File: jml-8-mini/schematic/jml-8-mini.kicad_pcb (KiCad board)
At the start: 4 copper layers, 136.4 x 81.5 mm, 50 parts, among them J1 BarrelJack, J2 SIO CHB, J3 UART, J4 CTC Extra Lines, J5 Address Decoding, J6 Z80 Lines, SW1 Reset, SW2 Power, U1 Z80CPU, U10 74LS74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

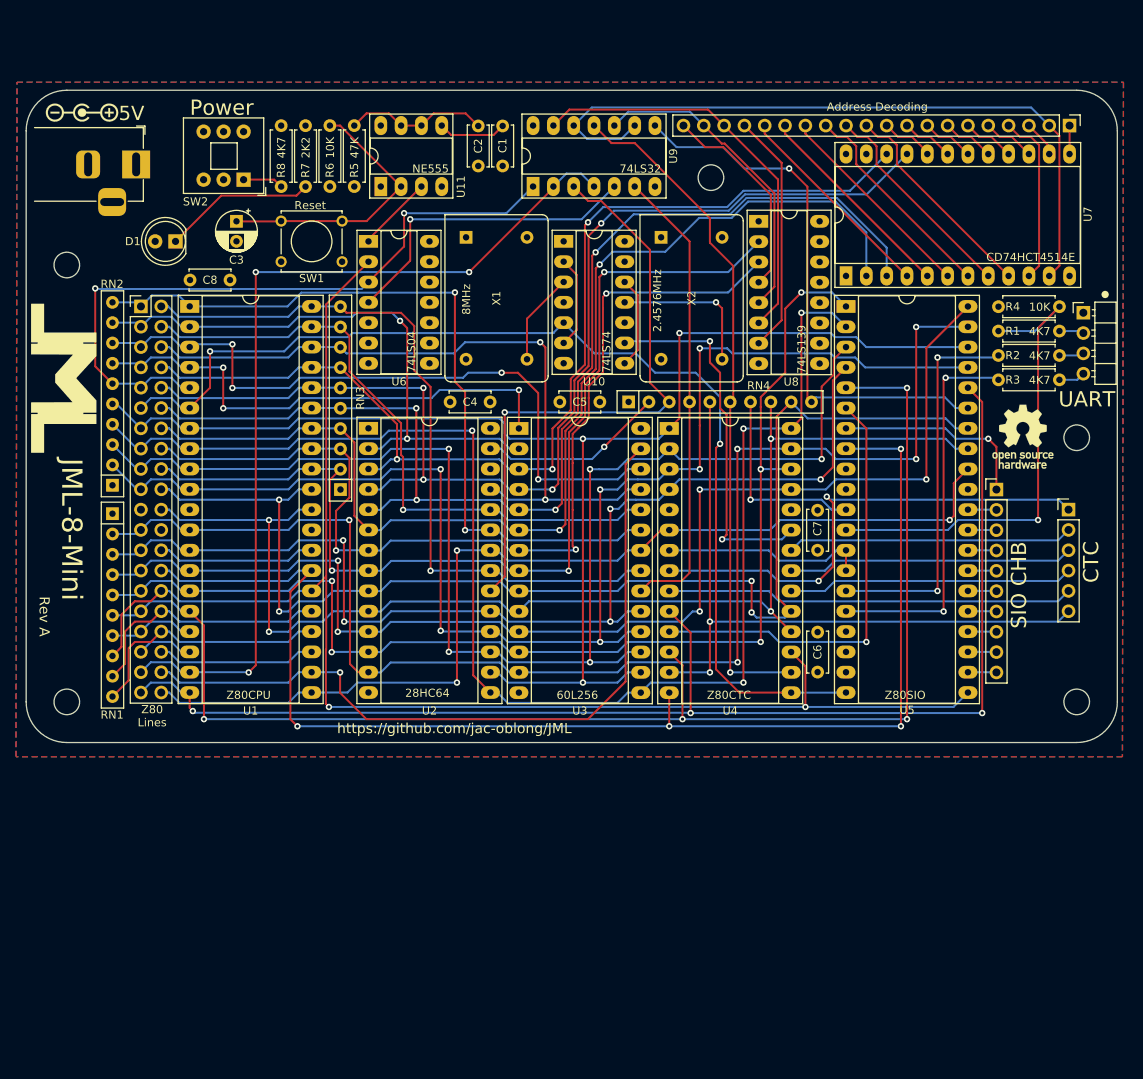
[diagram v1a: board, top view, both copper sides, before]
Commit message: Rev B, change dimensions of PCB for reduced cost
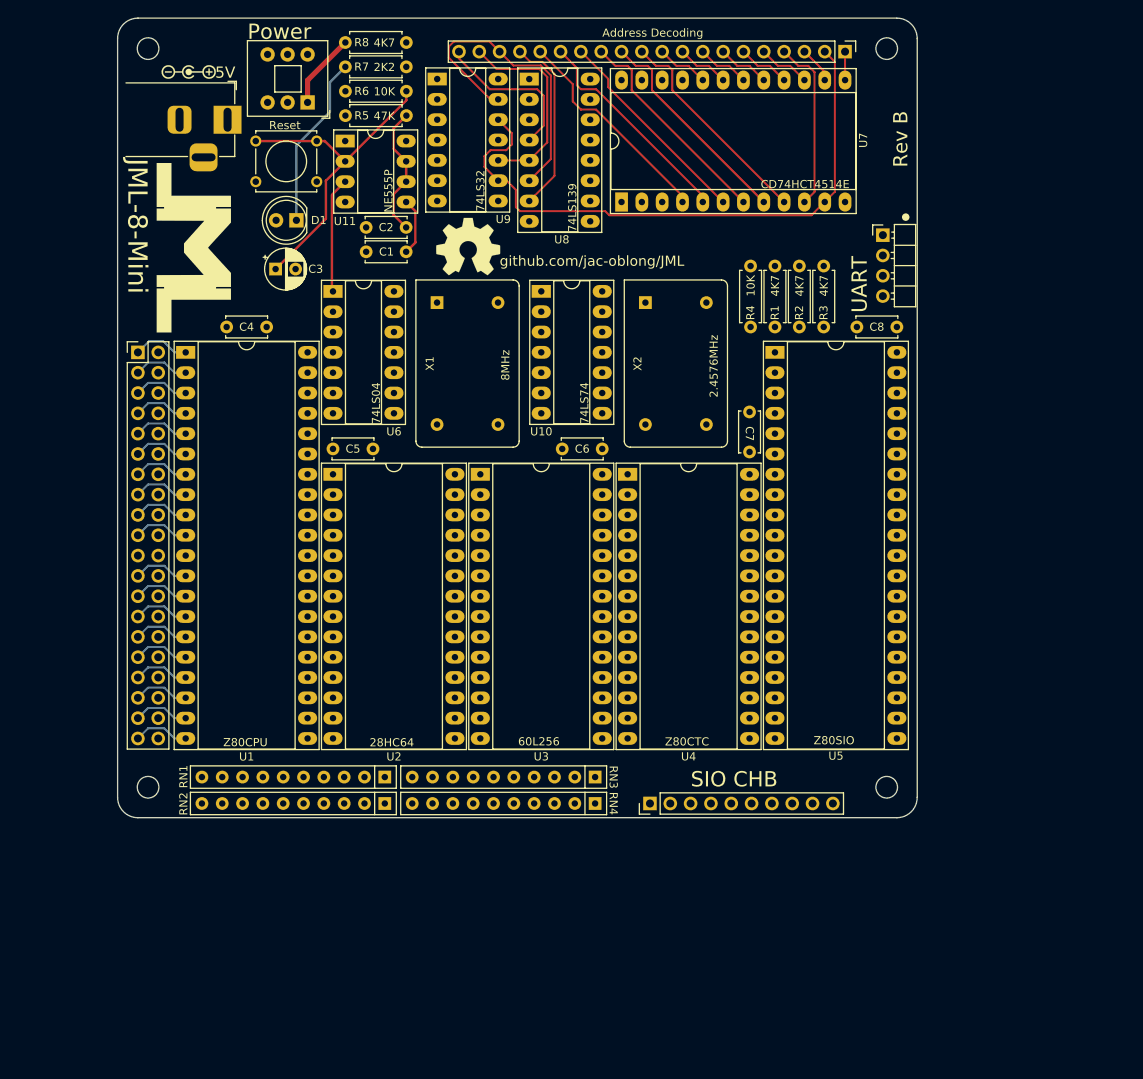
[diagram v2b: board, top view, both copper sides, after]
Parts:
- removed H5: MountingHole, MountingHole:MountingHole_3.2mm_M3
- removed J4: CTC Extra Lines, Connector_PinHeader_2.54mm:PinHeader_1x06_P2.54mm_Vertical
- removed the REF** at (208.4, 93.3)
- added REF**: OSHW-Symbol_8.9x8mm_SilkScreen, Symbol:OSHW-Symbol_8.9x8mm_SilkScreen, F.Cu at (139.1, 69.6)
- H1, H2, H3, H4: footprint MountingHole:MountingHole_3.2mm_M3 -> MountingHole:MountingHole_2.7mm_M2.5
- moved H1 125.9 mm to (99.1, 44.8)
- moved H4 103.0 mm to (191.4, 137.2)
- moved C8 83.6 mm to (192.7, 79.6)
- moved H3 66.1 mm to (99.1, 137.2)
- moved J2 58.4 mm to (161.8, 139.2), turned to 90 degrees
- moved RN2 52.4 mm to (128.7, 139.2), turned to 180 degrees
- moved RN4 50.4 mm to (154.9, 139.2), turned to 180 degrees
- moved RN3 48.0 mm to (154.9, 135.9), turned to 180 degrees
- moved RN1 47.4 mm to (128.7, 135.9), turned to 180 degrees
- moved C6 38.8 mm to (155.8, 94.9), turned to 180 degrees
- moved R1 36.5 mm to (177.4, 72.0), turned to -90 degrees
- moved R2 34.4 mm to (180.5, 72.0), turned to -90 degrees
- moved U8 33.7 mm to (146.7, 48.6)
- moved R3 32.7 mm to (183.5, 72.0), turned to -90 degrees
- moved R4 31.1 mm to (174.4, 79.6), turned to 90 degrees
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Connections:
- U4 pad 20: /Peripherals/CLK/TRG3 -> unconnected-(U4-CLK/TRG3-Pad20)
- U4 pad 21: /Peripherals/CLK/TRG2 -> unconnected-(U4-CLK/TRG2-Pad21)
- U4 pad 22: /Peripherals/CLK/TRG1 -> unconnected-(U4-CLK/TRG1-Pad22)
- U4 pad 8: /Peripherals/ZC/TO1 -> unconnected-(U4-ZC/TO1-Pad8)
- U4 pad 9: /Peripherals/ZC/TO2 -> unconnected-(U4-ZC/TO2-Pad9)
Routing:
- net /~{RESET}: track 180.4 -> 0.00 mm, vias 2 -> 0
- net /D4: track 174.3 -> 7.02 mm, vias 3 -> 0
- net /D3: track 174.1 -> 7.02 mm, vias 4 -> 0
- net /D6: track 172.9 -> 7.02 mm, vias 6 -> 0
- net /D2: track 172.4 -> 7.02 mm, vias 5 -> 0
- net /~{INT}: track 171.1 -> 7.02 mm, vias 4 -> 0
- net /~{M1}: track 162.0 -> 0.00 mm, vias 4 -> 0
- net /D5: track 165.7 -> 7.02 mm, vias 5 -> 0
- net /~{IORQ}: track 163.6 -> 7.02 mm, vias 3 -> 0
- net /A1: track 156.1 -> 0.00 mm, vias 4 -> 0
- net /A0: track 154.6 -> 0.00 mm, vias 4 -> 0
- net /A5: track 148.6 -> 0.00 mm, vias 4 -> 0
- net /A6: track 147.2 -> 0.00 mm, vias 4 -> 0
- net /D0: track 154.1 -> 7.02 mm, vias 5 -> 0
- net /D1: track 149.2 -> 7.02 mm, vias 5 -> 0
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- removed copper zone on B.Cu, net GND
- removed copper zone on F.Cu, net GND
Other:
- board size 136.4 x 81.5 mm -> 99.9 x 99.9 mm
- board text added: "Rev B"
- board text added: "github.com/jac-oblong/JML"
- board text added: "~{W}"
- board text removed: "18"
- board text removed: "2.4576MHz"
- board text removed: "21"
- board text removed: "28HC64"
- board text removed: "30"
- board text removed: "60L256"
- board text removed: "74LS04"
- board text removed: "74LS139"
- board text removed: "74LS32"
- board text removed: "74LS74"
- board text removed: "8MHz"
- board text removed: "CD74HCT4514E"
- board text removed: "CLK1"
- board text removed: "CLK2"
- board text removed: "CLK3"
- board text removed: "CTC"
- board text removed: "IEI"
- board text removed: "NE555"
- board text removed: "Rev A"
- board text removed: "Z80 Lines"
- board text removed: "Z80CPU"
- board text removed: "Z80CTC"
- board text removed: "Z80SIO"
- board text removed: "ZC1"
- board text removed: "ZC2"
- board text removed: "https://github.com/jac-oblong/JML"
- board text removed: "~{W}/~{RDY}"

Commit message: more updates for new PCB design
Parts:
- moved RN1 30.6 mm to (128.7, 166.5)
- moved RN3 30.6 mm to (154.9, 166.5)
- moved RN2 30.6 mm to (128.7, 169.8)
- moved RN4 30.6 mm to (154.9, 169.8)
- moved J3 0.06 mm to (190.9, 68.2)
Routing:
- net /~{IORQ}: track 7.02 -> 152.1 mm, vias 0 -> 4
- net /~{MREQ}: track 7.02 -> 111.7 mm, vias 0 -> 1
- net /~{CTC}: track 0.00 -> 102.7 mm, vias 0 -> 1
- net /A9: track 0.00 -> 92.8 mm, vias 0 -> 2
- net /A8: track 0.00 -> 84.6 mm, vias 0 -> 2
- net /D3: track 7.02 -> 91.1 mm, vias 0 -> 2
- net /D4: track 7.02 -> 90.9 mm, vias 0 -> 4
- net /A11: track 7.13 -> 88.4 mm, vias 0 -> 2
- net /~{RD}: track 0.00 -> 79.6 mm, vias 0 -> 2
- net /~{SIO}: track 0.00 -> 79.4 mm, vias 0 -> 2
- net /A15: track 7.02 -> 84.5 mm, vias 0 -> 2
- net /D5: track 7.02 -> 83.2 mm, vias 0 -> 4
- net /~{RAM}: track 0.00 -> 72.2 mm, vias 0 -> 1
- net /D6: track 7.02 -> 77.7 mm, vias 0 -> 2
- net /~{ROM}: track 0.00 -> 69.5 mm, vias 0 -> 1
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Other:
- board text added: "RN should move vertically only (stay the same horizontally)"
- board text added: "should line up with top of RN courtyard"

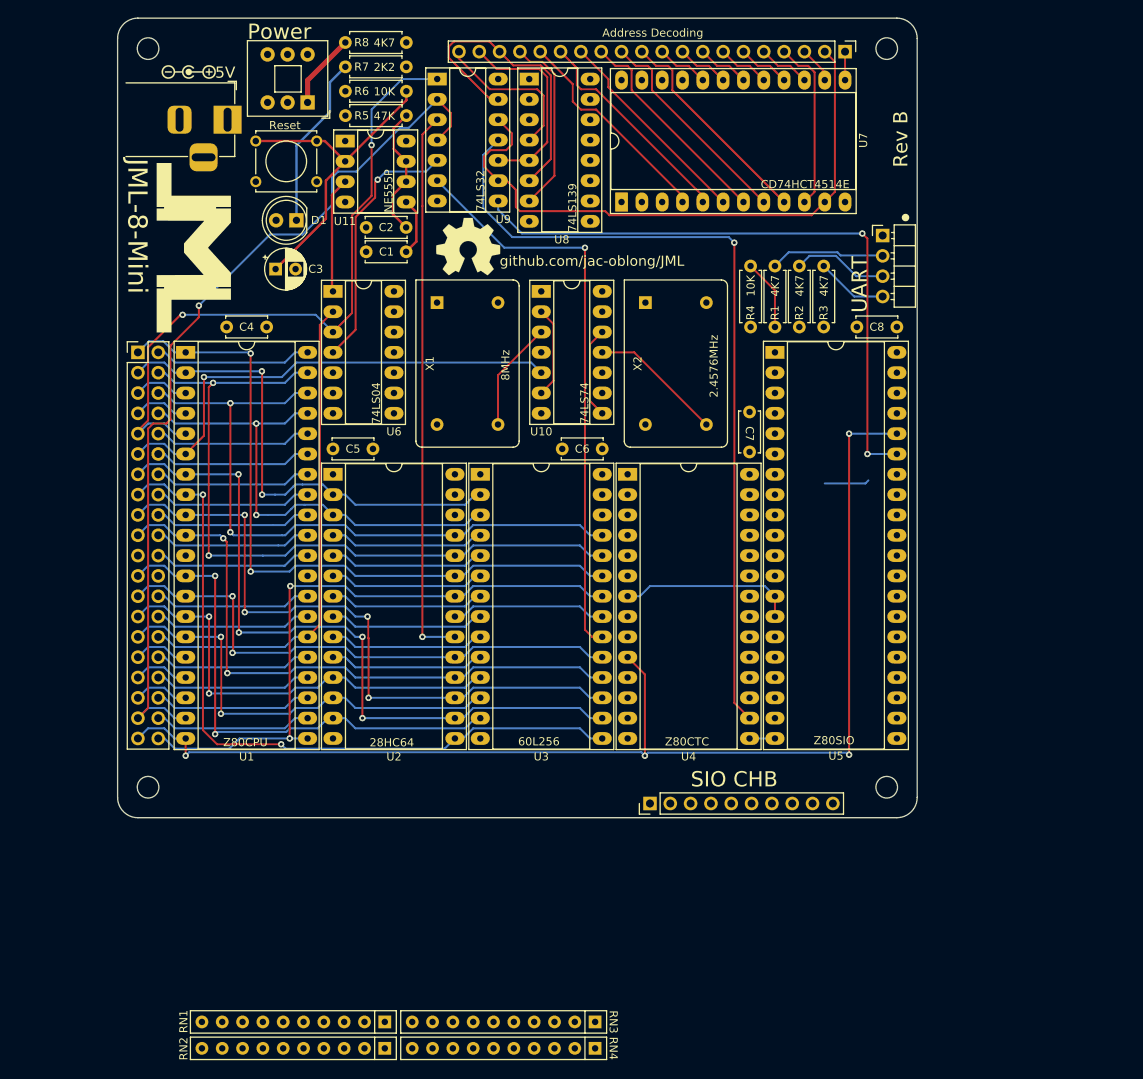
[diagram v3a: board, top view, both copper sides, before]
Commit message: finish rerouting PCB for Rev B
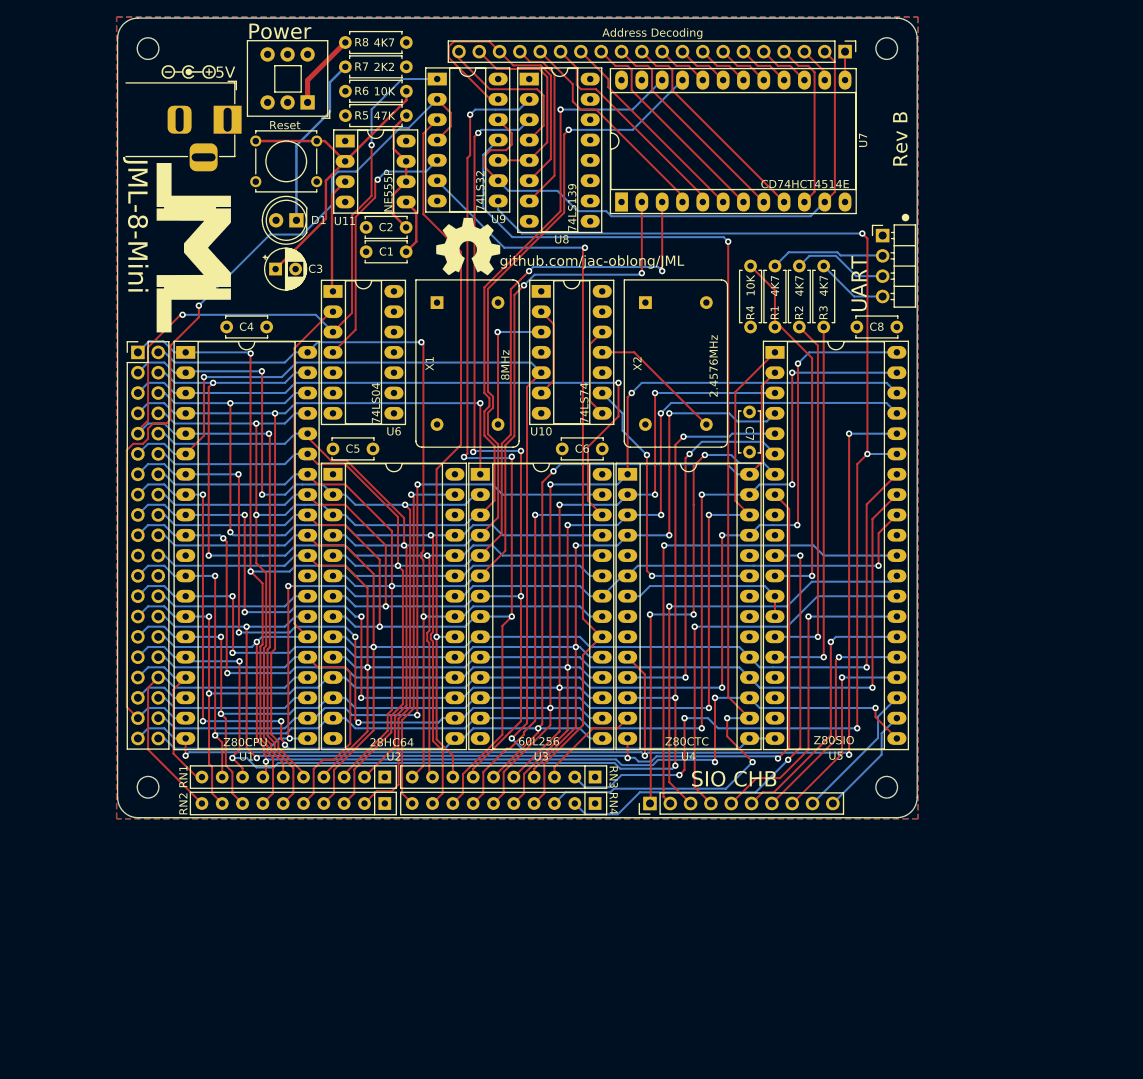
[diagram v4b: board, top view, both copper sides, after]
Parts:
- moved RN1 30.6 mm to (128.7, 135.9)
- moved RN3 30.6 mm to (154.9, 135.9)
- moved RN2 30.6 mm to (128.7, 139.2)
- moved RN4 30.6 mm to (154.9, 139.2)
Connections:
- RN1 pad 10: /~{WAIT} -> /~{NMI}
- RN1 pad 2: /D2 -> /A6
- RN1 pad 3: /D7 -> /A4
- RN1 pad 4: /D0 -> /A0
- RN1 pad 5: /D1 -> /A14
- RN1 pad 6: /~{INT} -> /A7
- RN1 pad 7: /~{NMI} -> /~{RESET}
- RN1 pad 8: /~{RESET} -> /~{INT}
- RN1 pad 9: /~{BUSRQ} -> /D2
- RN2 pad 10: /A11 -> /~{WAIT}
- RN2 pad 2: /D6 -> /A12
- RN2 pad 3: /D5 -> /A5
- RN2 pad 4: /D3 -> /A1
- RN2 pad 5: /D4 -> /~{BUSRQ}
- RN2 pad 7: /A14 -> /A11
- RN2 pad 8: /A13 -> /D1
- RN2 pad 9: /A12 -> /D0
- RN3 pad 2: /A2 -> /~{SIO}
- RN3 pad 3: /A3 -> /CTC IEI
- RN3 pad 4: /A4 -> /D7
- RN3 pad 5: /A5 -> /D5
- RN3 pad 6: /A6 -> /D3
- RN3 pad 7: /A7 -> /A3
- RN3 pad 8: /A8 -> /~{ROM}
- RN4 pad 10: /~{SIO} -> /~{ROM WE}
- RN4 pad 2: /~{ROM WE} -> /~{SIO SYNCA}
- RN4 pad 3: /~{ROM} -> /~{CTC}
- RN4 pad 5: /CTC IEI -> /D6
- RN4 pad 6: /~{CTC} -> /D4
- RN4 pad 7: /~{SIO SYNCA} -> /A13
- RN4 pad 8: /A0 -> /A2
- RN4 pad 9: /A1 -> /A8
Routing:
- net /~{INT}: track 7.02 -> 145.0 mm, vias 0 -> 5
- net /A2: track 39.2 -> 166.6 mm, vias 0 -> 5
- net /A6: track 39.2 -> 164.2 mm, vias 0 -> 2
- net /A3: track 39.2 -> 160.8 mm, vias 0 -> 5
- net /A13: track 7.02 -> 128.4 mm, vias 0 -> 2
- net /~{M1}: track 19.7 -> 139.4 mm, vias 0 -> 4
- net /A5: track 39.2 -> 156.6 mm, vias 0 -> 3
- net /A1: track 39.2 -> 156.3 mm, vias 0 -> 2
- net /A0: track 39.2 -> 150.2 mm, vias 0 -> 2
- net /A4: track 39.2 -> 148.7 mm, vias 0 -> 3
- net /~{RESET}: track 61.7 -> 171.2 mm, vias 0 -> 5
- net /D0: track 55.3 -> 162.7 mm, vias 2 -> 6
- net /A7: track 61.3 -> 166.3 mm, vias 2 -> 3
- net /D2: track 65.5 -> 167.6 mm, vias 2 -> 6
- net /D4: track 90.9 -> 189.0 mm, vias 4 -> 7
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- added copper zone on B.Cu, net GND
- added copper zone on F.Cu, net GND
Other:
- board text removed: "RN should move vertically only (stay the same horizontally)"
- board text removed: "should line up with top of RN courtyard"
